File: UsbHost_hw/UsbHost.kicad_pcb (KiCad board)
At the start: 2 copper layers, 79 x 16 mm, 41 parts

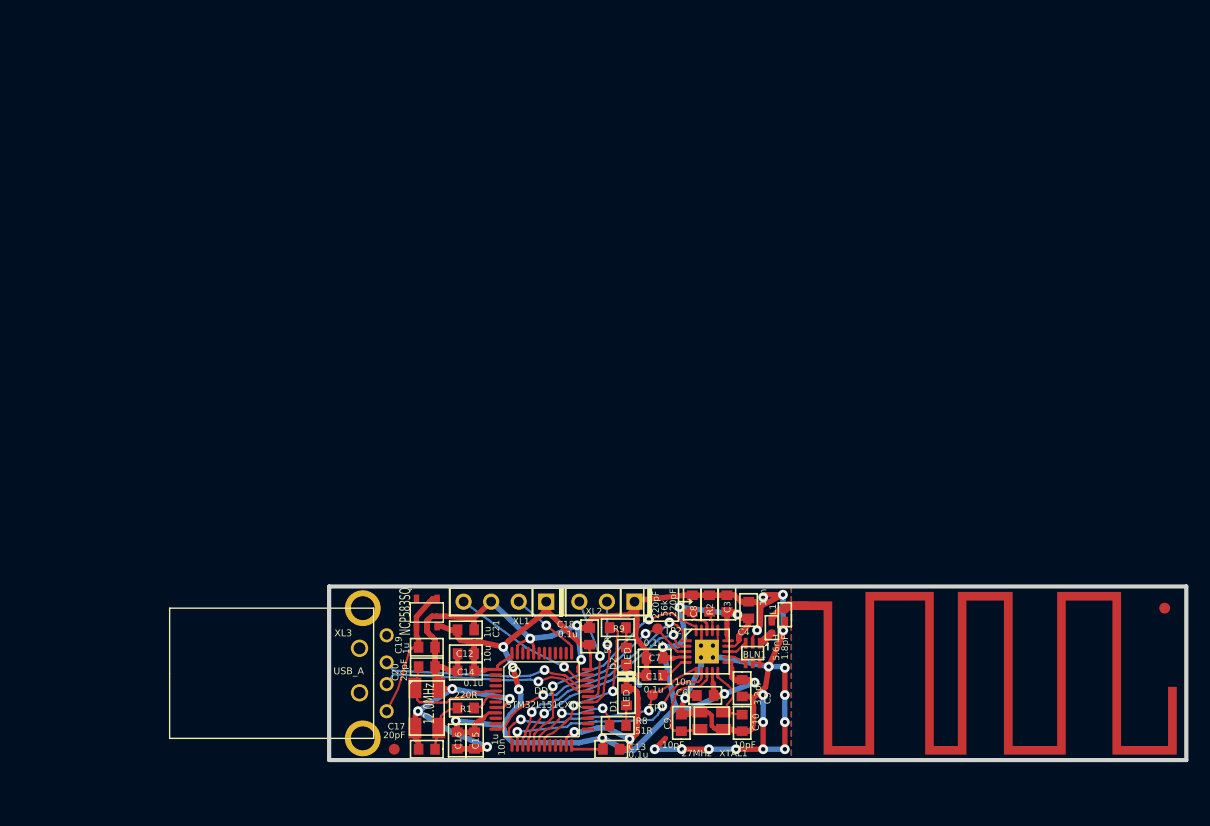
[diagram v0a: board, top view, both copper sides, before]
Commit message: + UsbHost2 hw
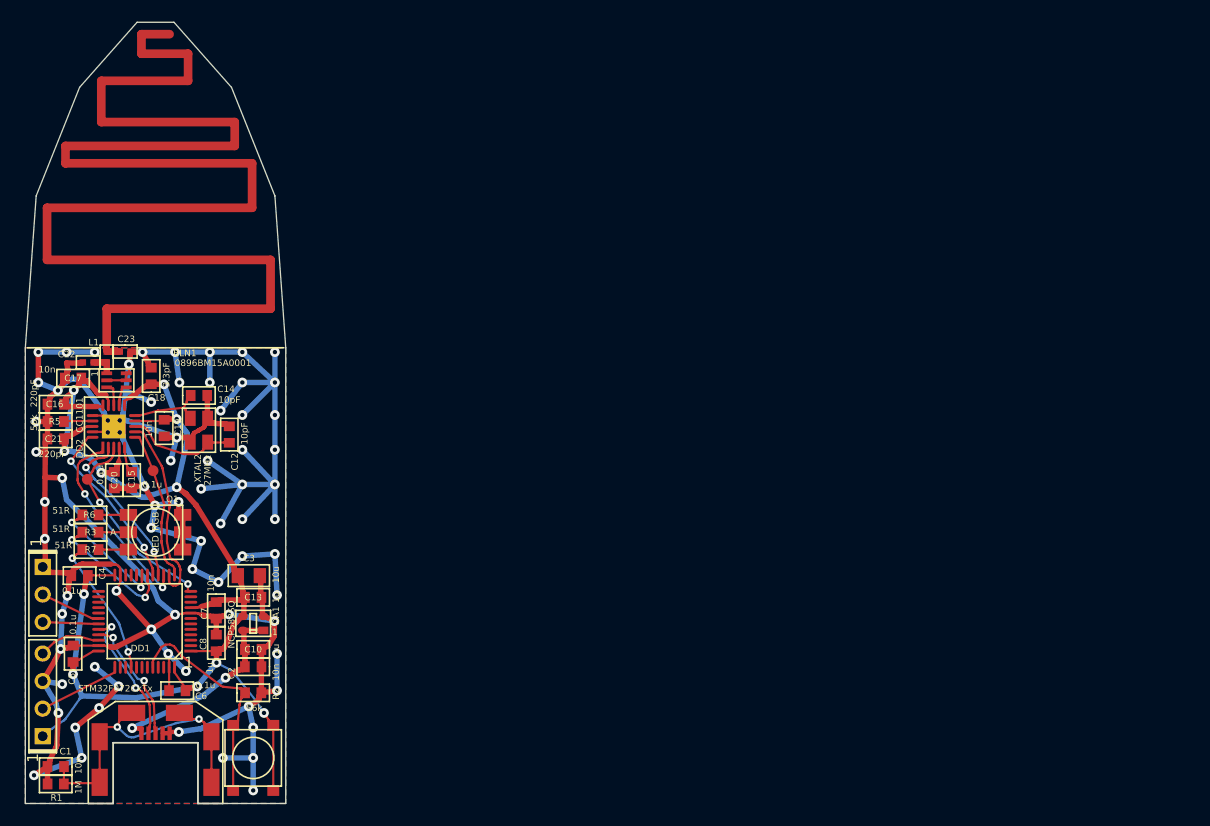
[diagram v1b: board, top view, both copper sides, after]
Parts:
- removed C11: 0.1u, CAP_0603
- removed C9: 10pF, CAP_0603
- removed D1, D2: LED, LED0603
- removed R8, R9: 51R, RES_0603
- removed RP1, RP2: REFPOINT, REF_POINT_1MM
- removed XTAL1: 27MHz, CRYSTAL_03225C4
- added C1: 10n, Capacitors:CAP_0603, F.Cu at (169.8, 189.6)
- added C22: 1.8pF, Capacitors:CAP_0402, F.Cu at (172.8, 152.3)
- added C23: 1.8pF, Capacitors:CAP_0402, F.Cu at (176.2, 151.3)
- added Q1: LED_RGB, LEDs:LED_5050, F.Cu at (179.0, 168.0)
- added R3: 51R, Resistors:RES_0603, F.Cu at (173.0, 168.0)
- added R5: 56k, Resistors:RES_0603, F.Cu at (169.8, 157.8)
- added R6: 51R, Resistors:RES_0603, F.Cu at (173.0, 166.4)
- added R7: 51R, Resistors:RES_0603, F.Cu at (173.0, 169.6)
- added SW1: BUTTON, BtnsSwitches:BTN_4x4_SMD, F.Cu at (188.0, 188.8)
- ANT1: footprint ANT_MEANDER868_16MM -> Radio:ANT_868_SEIDHE
- BLN1: footprint BALUN_JOHANSON868 -> Radio:BALUN_JOHANSON868
- C10: value 10pF -> 1u; footprint CAP_0603 -> Capacitors:CAP_0603
- C12: value 10u -> 10pF; footprint CAP_0603 -> Capacitors:CAP_0603
- C13: value 0.1u -> 1u; footprint CAP_0603 -> Capacitors:CAP_0603
- C14: value 0.1u -> 10pF; footprint CAP_0603 -> Capacitors:CAP_0603
- C15, C4, C6: value 10n -> 0.1u; footprint CAP_0603 -> Capacitors:CAP_0603
- C16, C21: value 1u -> 220pF; footprint CAP_0603 -> Capacitors:CAP_0603
- C17: value 20pF -> 10n; footprint CAP_0603 -> Capacitors:CAP_0603
- C18: value 0.1u -> 3.3pF; footprint CAP_0603 -> Capacitors:CAP_0603
- C19: value 1u -> 10n; footprint CAP_0603 -> Capacitors:CAP_0603
- C2: value 1.8pF -> 10n; footprint CAP_0402 -> Capacitors:CAP_0603
- C20: value 20pF -> 0.1u; footprint CAP_0603 -> Capacitors:CAP_0603
- C3: value 220pF -> 10u; footprint CAP_0603 -> Capacitors:CAP_0805
- C5: value 3.3pF -> 0.1u; footprint CAP_0603 -> Capacitors:CAP_0603
- C7: value 0.1u -> 10n; footprint CAP_0603 -> Capacitors:CAP_0603
- C8: value 220pF -> 1u; footprint CAP_0603 -> Capacitors:CAP_0603
- DA1: footprint SOT23-5 -> SOT:SC82AB
- DD1: value STM32L151CXTX -> STM32F072CxTx; footprint LQFP48 -> LQFP_TQFP:LQFP48
- DD2: footprint QFN20 -> QFN_DFN:QFN20
- L1: footprint IND_0402 -> Inductors:IND_0402
- R1: value 220R -> 1M; footprint RES_0603 -> Resistors:RES_0603
- R2: footprint RES_0603 -> Resistors:RES_0603
- TP1, TP2: footprint TESTPOINT_1MM -> PCB:TESTPOINT_1MM
- XL1: value ST_SWD -> CONN_3; footprint CONN_PLS-4 -> Connectors:PLS-3
- XL2: value CONN_3 -> ST_SWD; footprint CONN_PLS-3 -> Connectors:PLS-4
- XL3: value USB_A -> USB_MINI_B; footprint USB_AM -> Connectors:USBmicro_MOLEX_WM17142
- XTAL2: value 12.0MHz -> 27MHz; footprint CRYSTAL_0503x4-4 -> Quartz:03225C4
- moved L1 66.2 mm to (174.5, 151.8)
- moved ANT1 65.8 mm to (179.0, 151.0), turned to 90 degrees
- moved BLN1 63.8 mm to (175.4, 154.0), turned to 90 degrees
- moved C4 61.7 mm to (172.0, 172.0), turned to 180 degrees
- moved C5 61.7 mm to (171.4, 179.2), turned to 90 degrees
- moved DD2 58.5 mm to (175.2, 158.2), turned to 90 degrees
- moved TP2 54.3 mm to (172.7, 163.1), turned to 90 degrees
- moved XL2 53.5 mm to (168.6, 186.8), turned to 90 degrees
- moved TP1 50.5 mm to (178.8, 162.3), turned to 90 degrees
- moved C2 49.2 mm to (188.0, 180.4), turned to 180 degrees
- moved C6 48.7 mm to (181.0, 182.6)
- moved C16 48.3 mm to (169.8, 156.2), turned to 180 degrees
- moved C17 47.2 mm to (171.4, 153.8)
- moved C18 47.0 mm to (178.6, 153.6)
- moved C10 45.6 mm to (188.0, 178.8), turned to 0 degrees
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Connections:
- net /USB_DM renamed /D-
- net /USB_DP renamed /D+
- ANT1 pad 1: N-0000022 -> Net-(ANT1-Pad1)
- C10 pad 1: N-0000043 -> +5V
- C12 pad 1: +3.3V -> Net-(C12-Pad1)
- C14 pad 1: +3.3V -> Net-(C14-Pad1)
- C15 pad 1: +3.3V -> Net-(C15-Pad1)
- C17 pad 1: N-0000035 -> +3.3V
- C19 pad 1: +5V -> +3.3V
- C2 pad 1: N-0000022 -> GND
- C2 pad 2: GND -> +5V
- C20 pad 1: N-0000037 -> +3.3V
- DD1 pad 18: /LED1 -> /LED_R
- DD1 pad 19: /LED2 -> /LED_G
- DD1 pad 40: (no net) -> /LED_B
- DD1 pad 44: GND -> Net-(DD1-Pad44)
- DD1 pad 5: N-0000037 -> (no net)
- DD1 pad 6: N-0000036 -> (no net)
- DD2 pad 10: N-0000043 -> Net-(C14-Pad1)
- DD2 pad 17: N-0000025 -> Net-(DD2-Pad17)
- DD2 pad 5: N-0000040 -> Net-(C15-Pad1)
- DD2 pad 8: N-0000050 -> Net-(C12-Pad1)
- L1 pad 1: N-0000022 -> Net-(ANT1-Pad1)
- R1 pad 1: N-0000036 -> /SHLD
- R1 pad 2: N-0000035 -> GND
- R2 pad 1: N-0000025 -> Net-(DD1-Pad44)
- XL1 pad 1: +3.3V -> GND
- XL1 pad 2: /SWCLK -> /UART_TX
- XL1 pad 3: GND -> /UART_RX
- XL2 pad 1: GND -> +3.3V
- XL2 pad 2: /UART_TX -> /SWCLK
- XL2 pad 3: /UART_RX -> GND
- XL3 pad SHLD: GND -> /SHLD
- XTAL2 pad 1: N-0000037 -> Net-(C12-Pad1)
- XTAL2 pad 2: N-0000035 -> Net-(C14-Pad1)
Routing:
- net GND: track 185.4 -> 327.8 mm, vias 27 -> 71
- net /SHLD: track 0.00 -> 29.5 mm, vias 0 -> 2
- net Net-(DD1-Pad44): track 0.00 -> 20.8 mm
- net +3.3V: track 121.0 -> 141.8 mm, vias 10 -> 11
- net /LED2: track 15.1 -> 0.00 mm, vias 2 -> 0
- net /LED_B: track 0.00 -> 12.9 mm, vias 0 -> 2
- net /LED_R: track 0.00 -> 12.0 mm, vias 0 -> 2
- net /LED_G: track 0.00 -> 11.1 mm, vias 0 -> 2
- net N-0000037: track 10.7 -> 0.00 mm
- net Net-(C12-Pad1): track 0.00 -> 10.3 mm
- net N-0000050: track 9.89 -> 0.00 mm
- net /LED1: track 9.47 -> 0.00 mm, vias 2 -> 0
- net /SWDIO: track 13.8 -> 5.75 mm, vias 1 -> 0
- net /D+: track 19.5 -> 11.6 mm, vias 1 -> 2
- net /CC_GDO0: track 21.6 -> 14.0 mm, vias 2 -> 0
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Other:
- board size 79 x 16 mm -> 24 x 72 mm
- net class Default: via_dia 0.9 -> 0.7; via_drill 0.4 -> 0.3
- rule via_min_size: 0.9 -> 0.7
